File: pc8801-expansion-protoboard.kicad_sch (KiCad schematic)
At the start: 13 parts, among them J1 SD card, SW1 Reset ESP, U1 ExpansionEdge, U11 ESP32-DEVKITC

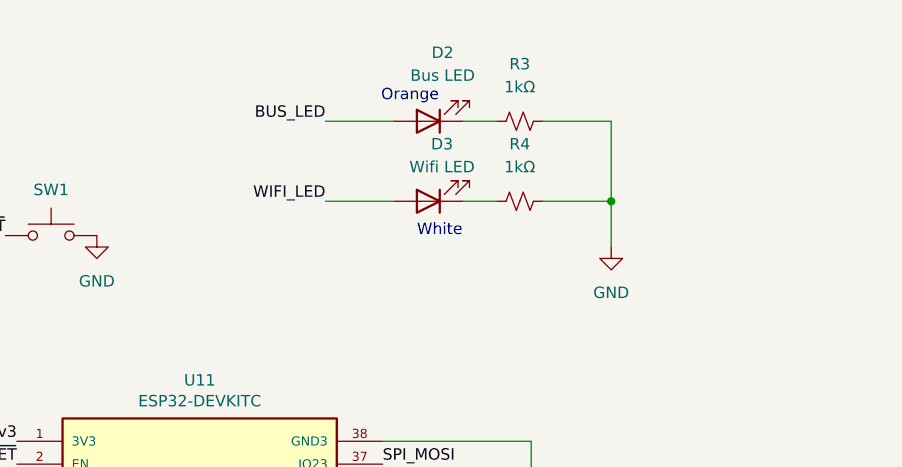
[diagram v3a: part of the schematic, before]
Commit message: Add Button A
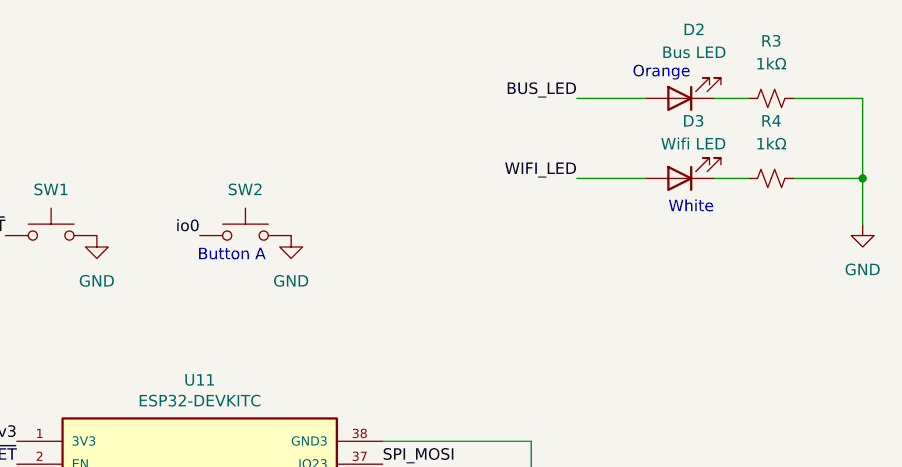
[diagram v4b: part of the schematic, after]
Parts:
- added SW2: Button A, Button_Switch_THT:SW_PUSH_6mm, symbol Switch:SW_Push
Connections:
- net GND: now also SW2.2
- net io0: now also SW2.1
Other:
- note added: "Button A"
- moved on the sheet: D2, D3, R3, R4
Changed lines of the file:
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@@
 	)
 	(junction
-		(at 368.3 39.37)
+		(at 396.24 36.83)
 		(diameter 0)
 		(color 0 0 0 0)
@@
 	(wire
 		(pts
-			(xy 351.79 39.37) (xy 355.6 39.37)
+			(xy 379.73 36.83) (xy 383.54 36.83)
 		)
 		(stroke
@@
 	(wire
 		(pts
-			(xy 360.68 39.37) (xy 368.3 39.37)
+			(xy 388.62 36.83) (xy 396.24 36.83)
 		)
 		(stroke
@@
 	(wire
 		(pts
-			(xy 351.79 30.48) (xy 355.6 30.48)
+			(xy 379.73 27.94) (xy 383.54 27.94)
 		)
 		(stroke
@@
 	(wire
 		(pts
-			(xy 360.68 30.48) (xy 368.3 30.48)
+			(xy 388.62 27.94) (xy 396.24 27.94)
 		)
 		(stroke
@@
 	(wire
 		(pts
-			(xy 368.3 30.48) (xy 368.3 39.37)
+			(xy 396.24 27.94) (xy 396.24 36.83)
 		)
 		(stroke
@@
 	(wire
 		(pts
-			(xy 368.3 39.37) (xy 368.3 44.45)
+			(xy 396.24 36.83) (xy 396.24 41.91)
 		)
 		(stroke
@@
 	(wire
 		(pts
-			(xy 336.55 39.37) (xy 344.17 39.37)
+			(xy 364.49 36.83) (xy 372.11 36.83)
 		)
 		(stroke
@@
 	(wire
 		(pts
-			(xy 336.55 30.48) (xy 344.17 30.48)
+			(xy 364.49 27.94) (xy 372.11 27.94)
 		)
 		(stroke
@@
 	(text "White"
 		(exclude_from_sim no)
-		(at 349.25 42.672 0)
+		(at 377.19 40.132 0)
 		(effects
 			(font
@@
 		)
 	)
+	(text "Button A"
+		(exclude_from_sim no)
+		(at 326.136 45.466 0)
+		(effects
+			(font
+				(size 1.27 1.27)
+			)
+		)
+	)
 	(text "Orange"
 		(exclude_from_sim no)
-		(at 345.948 27.686 0)
+		(at 373.888 25.146 0)
 		(effects
 			(font
@@
 		)
 	)
+	(label "io0"
+		(at 322.58 43.18 180)
+		(fields_autoplaced yes)
+		(effects
+			(font
+				(size 1.27 1.27)
+			)
+			(justify right bottom)
+		)
+	)
 	(label "AB7"
 		(at 54.61 86.36 180)
@@
 	)
 	(label "BUS_LED"
-		(at 336.55 30.48 180)
+		(at 364.49 27.94 180)
 		(fields_autoplaced yes)
 		(effects
@@
 	)
 	(label "WIFI_LED"
-		(at 336.55 39.37 180)
+		(at 364.49 36.83 180)
 		(fields_autoplaced yes)
 		(effects
@@
 	)
 	(symbol
+		(lib_id "Switch:SW_Push")
+		(at 327.66 43.18 0)
+		(unit 1)
+		(exclude_from_sim no)
+		(in_bom yes)
+		(on_board yes)
+		(dnp no)
+		(fields_autoplaced yes)
+		(property "Reference" "SW2"
+			(at 327.66 38.1 0)
+			(effects
+				(font
+					(size 1.27 1.27)
+				)
+			)
+		)
+		(property "Value" "Button A"
+			(at 327.66 38.1 0)
+			(effects
+				(font
+					(size 1.27 1.27)
+				)
+				(hide yes)
+			)
+		)
+		(property "Footprint" "Button_Switch_THT:SW_PUSH_6mm"
+			(at 327.66 38.1 0)
+			(effects
+				(font
+					(size 1.27 1.27)
+				)
+				(hide yes)
+			)
+		)
+		(property "Datasheet" "~"
+			(at 327.66 38.1 0)
+			(effects
+				(font
+					(size 1.27 1.27)
+				)
+				(hide yes)
+			)
+		)
+		(property "Description" "Push button switch, generic, two pins"
+			(at 327.66 43.18 0)
+			(effects
+				(font
+					(size 1.27 1.27)
+				)
+				(hide yes)
+			)
+		)
+		(pin "2"
+		)
+		(pin "1"
+		)
+		(instances
+			(project "pc8801-expansion-protoboard"
+				(path "/5ff4411a-6b33-4619-8d94-dd770b3117b7"
+					(reference "SW2")
+					(unit 1)
+				)
+			)
+		)
+	)
+	(symbol
 		(lib_id "Device:C_Polarized_Small_US")
 		(at 331.47 201.93 0)
@@
 	(symbol
 		(lib_id "Device:R_Small_US")
-		(at 358.14 39.37 90)
+		(at 386.08 36.83 90)
 		(unit 1)
 		(exclude_from_sim no)
@@
 		(fields_autoplaced yes)
 		(property "Reference" "R4"
-			(at 358.14 33.02 90)
+			(at 386.08 30.48 90)
 			(effects
 				(font
@@
 		)
 		(property "Value" "1kΩ"
-			(at 358.14 35.56 90)
+			(at 386.08 33.02 90)
 			(effects
 				(font
@@
 		)
 		(property "Footprint" ""
-			(at 358.14 39.37 0)
+			(at 386.08 36.83 0)
 			(effects
 				(font
@@
 		)
 		(property "Datasheet" "~"
-			(at 358.14 39.37 0)
+			(at 386.08 36.83 0)
 			(effects
 				(font
@@
 		)
 		(property "Description" "Resistor, small US symbol"
-			(at 358.14 39.37 0)
+			(at 386.08 36.83 0)
 			(effects
 				(font
@@
 				(path "/5ff4411a-6b33-4619-8d94-dd770b3117b7"
 					(reference "R4")
+					(unit 1)
+				)
+			)
+		)
+	)
+	(symbol
+		(lib_id "power:GND")
+		(at 332.74 43.18 0)
+		(unit 1)
+		(exclude_from_sim no)
+		(in_bom yes)
+		(on_board yes)
+		(dnp no)
+		(fields_autoplaced yes)
+		(property "Reference" "#PWR08"
+			(at 332.74 49.53 0)
+			(effects
+				(font
+					(size 1.27 1.27)
+				)
+				(hide yes)
+			)
+		)
+		(property "Value" "GND"
+			(at 332.74 48.26 0)
+			(effects
+				(font
+					(size 1.27 1.27)
+				)
+			)
+		)
+		(property "Footprint" ""
+			(at 332.74 43.18 0)
+			(effects
+				(font
+					(size 1.27 1.27)
+				)
+				(hide yes)
+			)
+		)
+		(property "Datasheet" ""
+			(at 332.74 43.18 0)
+			(effects
+				(font
+					(size 1.27 1.27)
+				)
+				(hide yes)
+			)
+		)
+		(property "Description" "Power symbol creates a global label with name \"GND\" , ground"
+			(at 332.74 43.18 0)
+			(effects
+				(font
+					(size 1.27 1.27)
+				)
+				(hide yes)
+			)
+		)
+		(pin "1"
+		)
+		(instances
+			(project ""
+				(path "/5ff4411a-6b33-4619-8d94-dd770b3117b7"
+					(reference "#PWR08")
 					(unit 1)
 				)
@@
 	(symbol
 		(lib_id "Device:R_Small_US")
-		(at 358.14 30.48 90)
+		(at 386.08 27.94 90)
 		(unit 1)
 		(exclude_from_sim no)
@@
 		(fields_autoplaced yes)
 		(property "Reference" "R3"
-			(at 358.14 24.13 90)
+			(at 386.08 21.59 90)
 			(effects
 				(font
@@
 		)
 		(property "Value" "1kΩ"
-			(at 358.14 26.67 90)
+			(at 386.08 24.13 90)
 			(effects
 				(font
@@
 		)
 		(property "Footprint" ""
-			(at 358.14 30.48 0)
+			(at 386.08 27.94 0)
 			(effects
 				(font
@@
 		)
 		(property "Datasheet" "~"
-			(at 358.14 30.48 0)
+			(at 386.08 27.94 0)
 			(effects
 				(font
@@
 		)
 		(property "Description" "Resistor, small US symbol"
-			(at 358.14 30.48 0)
+			(at 386.08 27.94 0)
 			(effects
 				(font
@@
 	(symbol
 		(lib_id "Device:LED")
-		(at 347.98 39.37 180)
+		(at 375.92 36.83 180)
 		(unit 1)
 		(exclude_from_sim no)
@@
 		(dnp no)
 		(property "Reference" "D3"
-			(at 349.504 33.02 0)
+			(at 377.444 30.48 0)
 			(effects
 				(font
@@
 		)
 		(property "Value" "Wifi LED"
-			(at 349.504 35.56 0)
+			(at 377.444 33.02 0)
 			(effects
 				(font
@@
 		)
 		(property "Footprint" "LED_THT:LED_D3.0mm"
-			(at 347.98 39.37 0)
+			(at 375.92 36.83 0)
 			(effects
 				(font
@@
 		)
 		(property "Datasheet" "~"
-			(at 347.98 39.37 0)
+			(at 375.92 36.83 0)
 			(effects
 				(font
@@
 		)
 		(property "Description" "Light emitting diode, white"
-			(at 347.98 39.37 0)
+			(at 375.92 36.83 0)
 			(effects
 				(font
@@
 	(symbol
 		(lib_id "Device:LED")
-		(at 347.98 30.48 180)
+		(at 375.92 27.94 180)
 		(unit 1)
 		(exclude_from_sim no)
@@
 		(fields_autoplaced yes)
 		(property "Reference" "D2"
-			(at 349.5675 22.86 0)
+			(at 377.5075 20.32 0)
 			(effects
 				(font
@@
 		)
 		(property "Value" "Bus LED"
-			(at 349.5675 25.4 0)
+			(at 377.5075 22.86 0)
 			(effects
 				(font
@@
 		)
 		(property "Footprint" "LED_THT:LED_D3.0mm"
-			(at 347.98 30.48 0)
+			(at 375.92 27.94 0)
 			(effects
 				(font
@@
 		)
 		(property "Datasheet" "~"
-			(at 347.98 30.48 0)
+			(at 375.92 27.94 0)
 			(effects
 				(font
@@
 		)
 		(property "Description" "Light emitting diode, orange"
-			(at 347.98 30.48 0)
+			(at 375.92 27.94 0)
 			(effects
 				(font
@@
 	(symbol
 		(lib_id "power:GND")
-		(at 368.3 44.45 0)
+		(at 396.24 41.91 0)
 		(unit 1)
 		(exclude_from_sim no)
@@
 		(fields_autoplaced yes)
 		(property "Reference" "#PWR07"
-			(at 368.3 50.8 0)
+			(at 396.24 48.26 0)
 			(effects
 				(font
@@
 		)
 		(property "Value" "GND"
-			(at 368.3 49.53 0)
+			(at 396.24 46.99 0)
 			(effects
 				(font
@@
 		)
 		(property "Footprint" ""
-			(at 368.3 44.45 0)
+			(at 396.24 41.91 0)
 			(effects
 				(font
@@
 		)
 		(property "Datasheet" ""
-			(at 368.3 44.45 0)
+			(at 396.24 41.91 0)
 			(effects
 				(font
@@
 		)
 		(property "Description" "Power symbol creates a global label with name \"GND\" , ground"
-			(at 368.3 44.45 0)
-			(effects
-				(font
+			(at 396.24 41.91 0)
+			(effects
+				(font

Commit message: Throwing stuff at the wall
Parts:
- added J2: Debug (Pico Probe), Connector_PinHeader_2.54mm:PinHeader_1x03_P2.54mm_Horizontal, symbol Connector:Conn_01x03_Pin
- added U2: ~, AliExpress_Picos:Ultimate_Pico_RP2040, symbol AliExpress_Picos:Ultimate_Pico_RP2040
- SW1: value Reset ESP -> Reset Pico
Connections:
- net AB0: now also U2.1 (GPIO_0)
- net AB1: now also U2.2 (GPIO_1)
- net AB10: now also U2.12 (GPIO_10)
- net AB11: now also U2.13 (GPIO_11)
- net AB12: now also U2.14 (GPIO_12)
- net AB13: now also U2.16 (GPIO_13)
- net AB14: now also U2.17 (GPIO_14)
- net AB15: now also U2.18 (GPIO_15)
- net AB2: now also U2.3 (GPIO_2)
- net AB3: now also U2.4 (GPIO_3)
- net AB4: now also U2.5 (GPIO_4)
- net AB5: now also U2.7 (GPIO_5)
- net AB6: now also U2.8 (GPIO_6)
- net AB7: now also U2.9 (GPIO_7)
- net AB8: now also U2.10 (GPIO_8)
- net AB9: now also U2.11 (GPIO_9)
- net CMD: now also U2.31 (GPIO_A1)
- net DB0: now also U2.19 (GPIO_16)
- net DB1: now also U2.20 (GPIO_17)
- net DB2: now also U2.21 (GPIO_18)
- net DB3: now also U2.22 (GPIO_19)
- net DB4: now also U2.23 (GPIO_20)
- net DB5: now also U2.24 (GPIO_21)
- net DB6: now also U2.25 (GPIO_22)
- net DB7: now also U2.26 (GPIO_23)
- net GND: now also J2.2 (Pin_2), U2.15 (GND), U2.29 (AGND), U2.35 (GND), U2.38 (GND), U2.6 (GND), U2.B2 (GND)
- net INT: now also U2.28 (GPIO_25)
- net PROC: now also U2.30 (GPIO_A0)
- net ~{ESP_RESET}: now also U2.27 (GPIO_24); no longer SW1.1
- new net PICO_SWCLK: J2.1 (Pin_1), U2.B3 (SWCLK)
- new net PICO_SWDIO: J2.3 (Pin_3), U2.B4 (SWDIO)
- new net ~{PICO_RESET}: SW1.1, U2.34 (RUN)
- no-connect marks 4 -> 7
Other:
- note added: "TODO: Buffering (74lvc245?)"
- note added: "TODO: Z80 bus control"
- note added: "Using a purple pico for contiguous pins here"
